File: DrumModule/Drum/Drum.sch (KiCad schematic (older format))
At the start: 44 parts, among them J1 Barrel_Jack_Switch, J2 Barrel_Jack_Switch, J3 Conn_02x05_Odd_Even, J4 Barrel_Jack_Switch, J5 Barrel_Jack_Switch, Q1 MMBT3904, Q2 MMBT3904, U1 74HC74, U2 MIC5205-5.0YM5, U3 LM2904DR, U4 LM2904DR

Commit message: Worked on the Drum
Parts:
- removed C10, C11, C4, C5: 1uF, Capacitor_SMD:C_0805_2012Metric, symbol Device:C_Small
- removed C6, C8: 68nF, Capacitor_SMD:C_0805_2012Metric, symbol Device:C_Small
- removed C7, C9: 22nF, Capacitor_SMD:C_0805_2012Metric, symbol Device:C_Small
- removed J1, J2, J4, J5: Barrel_Jack_Switch, Eurocad:PJ301M-12, symbol Connector:Barrel_Jack_Switch
- removed Q1, Q2: MMBT3904, Package_TO_SOT_SMD:SOT-23, symbol Transistor_BJT:MMBT3904
- removed R1, R2: 100k, Resistor_SMD:R_0805_2012Metric, symbol Device:R_US
- removed R10, R15, R16, R17, R18, R5, R6, R7, R8, R9: 10k, Resistor_SMD:R_0805_2012Metric, symbol Device:R_US
- removed R11, R3, R4: 1M, Resistor_SMD:R_0805_2012Metric, symbol Device:R_US
- removed R12: 2k2, Resistor_SMD:R_0805_2012Metric, symbol Device:R_US
- removed R13: 4.7M, Resistor_SMD:R_0805_2012Metric, symbol Device:R_US
- removed R14: 1k, Resistor_SMD:R_0805_2012Metric, symbol Device:R_US
- removed unit 1 of U1
- removed unit 2 of U1
- removed U3, U4: LM2904DR, Package_SO:SOIC-8_3.9x4.9mm_P1.27mm, symbol Device:Opamp_Dual_Generic
- U2: symbol Regulator_Linear:MIC5205-5.0YM5 -> Drum-rescue:MIC5205-5.0YM5-Regulator_Linear
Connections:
- wire segments 180 -> 56

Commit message: Organized layout of drum, should be ready for routing.
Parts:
- removed C2: 1uF, Capacitor_SMD:C_0805_2012Metric, symbol Device:C_Small
- removed U1: 74HC74, Package_SO:SOIC-14_3.9x8.7mm_P1.27mm, symbol 74xx:74HC74
- U2: symbol Drum-rescue:MIC5205-5.0YM5-Regulator_Linear -> Drum-rescue:MIC5205-5.0YM5-Regulator_Linear-Drum-rescue
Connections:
- wire segments 56 -> 48
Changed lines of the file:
@@
 $EndDescr
 $Comp
-L 74xx:74HC74 U1
-U 3 1 5C782298
-P 2400 6500
-F 0 "U1" V 2050 6400 50  0000 L CNN
-F 1 "74HC74" V 2150 6350 50  0000 L CNN
-F 2 "Package_SO:SOIC-14_3.9x8.7mm_P1.27mm" H 2400 6500 50  0001 C CNN
-F 3 "74xx/74hc_hct74.pdf" H 2400 6500 50  0001 C CNN
-	3    2400 6500
-	1    0    0    -1
-$EndComp
-$Comp
-L Drum-rescue:MIC5205-5.0YM5-Regulator_Linear U2
+L Drum-rescue:MIC5205-5.0YM5-Regulator_Linear-Drum-rescue U2
 U 1 1 5C78249B
 P 2950 4950
@@
 	1    0    0    -1
 $EndComp
-Wire Wire Line
-	2400 6100 2400 6050
-Wire Wire Line
-	2400 6900 2400 6950
-$Comp
-L power:GND #PWR011
-U 1 1 5C784795
-P 2400 7150
-F 0 "#PWR011" H 2400 6900 50  0001 C CNN
-F 1 "GND" H 2405 6977 50  0000 C CNN
-F 2 "" H 2400 7150 50  0001 C CNN
-F 3 "" H 2400 7150 50  0001 C CNN
-	1    2400 7150
-	1    0    0    -1
-$EndComp
-Wire Wire Line
-	2400 6950 2750 6950
-Connection ~ 2400 6950
-Wire Wire Line
-	2400 6950 2400 7150
-Wire Wire Line
-	2750 6050 2400 6050
-Connection ~ 2400 6050
-Wire Wire Line
-	2400 6050 2400 5850
 Wire Wire Line
 	1200 5900 1200 6000
@@
 $EndComp
 $Comp
-L power:+5V #PWR010
-U 1 1 5C79170B
-P 2400 5850
-F 0 "#PWR010" H 2400 5700 50  0001 C CNN
-F 1 "+5V" H 2415 6023 50  0000 C CNN
-F 2 "" H 2400 5850 50  0001 C CNN
-F 3 "" H 2400 5850 50  0001 C CNN
-	1    2400 5850
-	1    0    0    -1
-$EndComp
-$Comp
-L Device:C_Small C2
-U 1 1 5C791734
-P 2750 6450
-F 0 "C2" H 2842 6496 50  0000 L CNN
-F 1 "1uF" H 2842 6405 50  0000 L CNN
-F 2 "Capacitor_SMD:C_0805_2012Metric" H 2750 6450 50  0001 C CNN
-F 3 "~" H 2750 6450 50  0001 C CNN
-	1    2750 6450
-	1    0    0    -1
-$EndComp
-Wire Wire Line
-	2750 6050 2750 6350
-Wire Wire Line
-	2750 6550 2750 6950
-$Comp
 L power:GND #PWR016

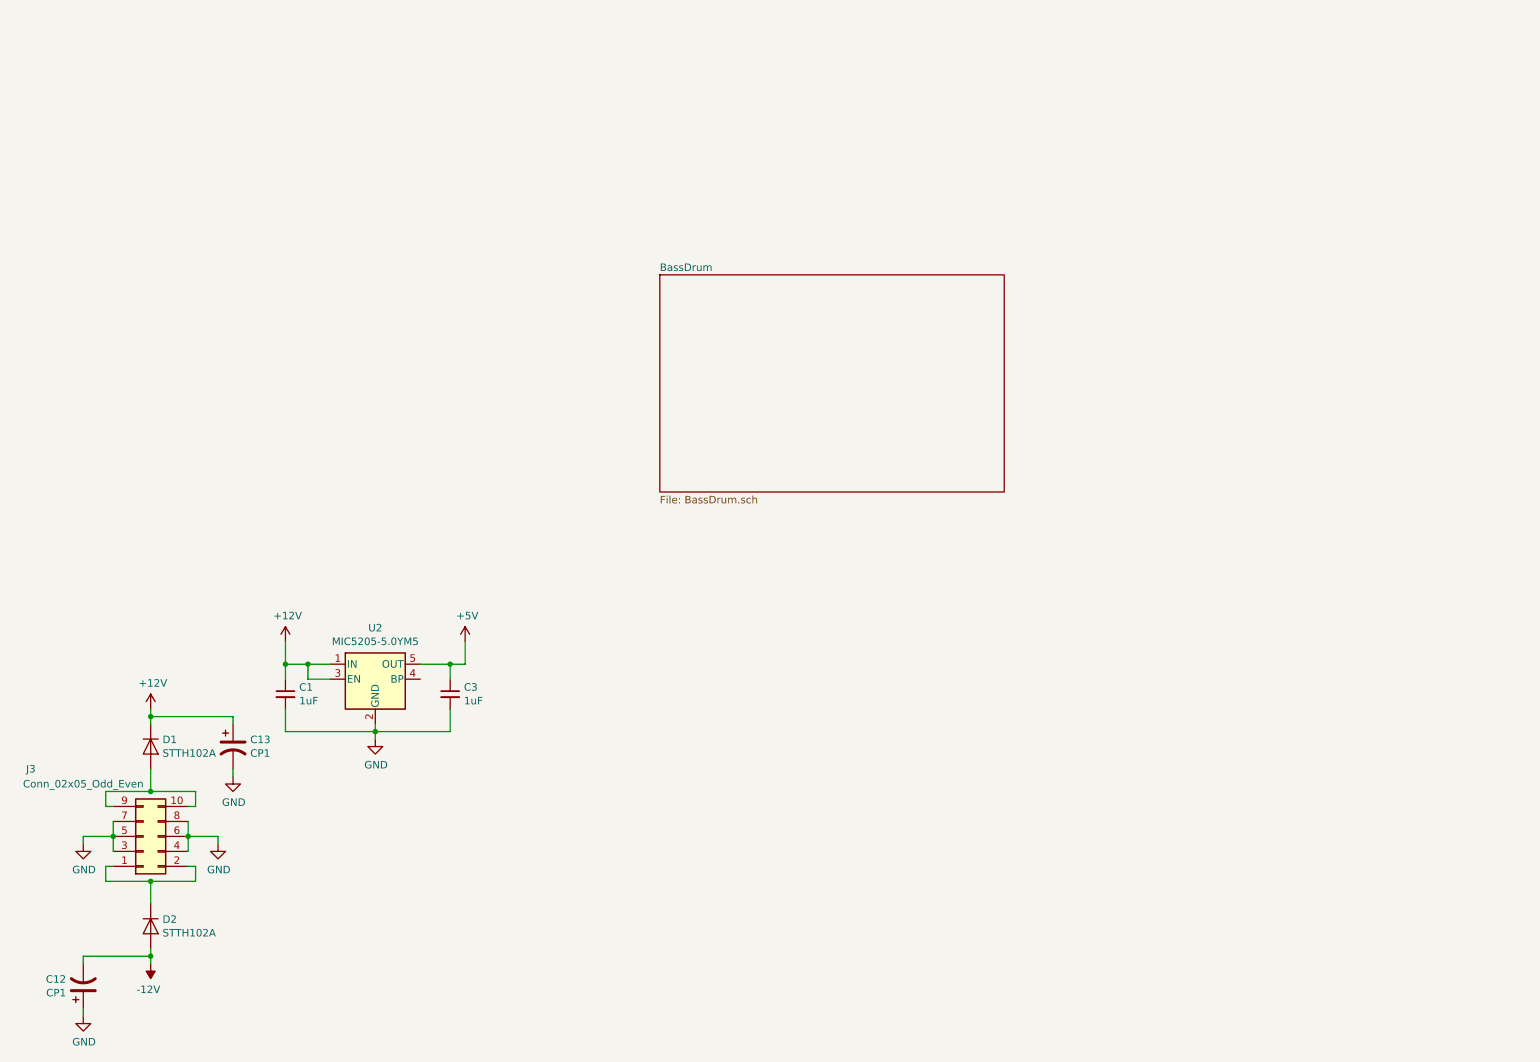
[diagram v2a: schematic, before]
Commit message: Finished off the drum
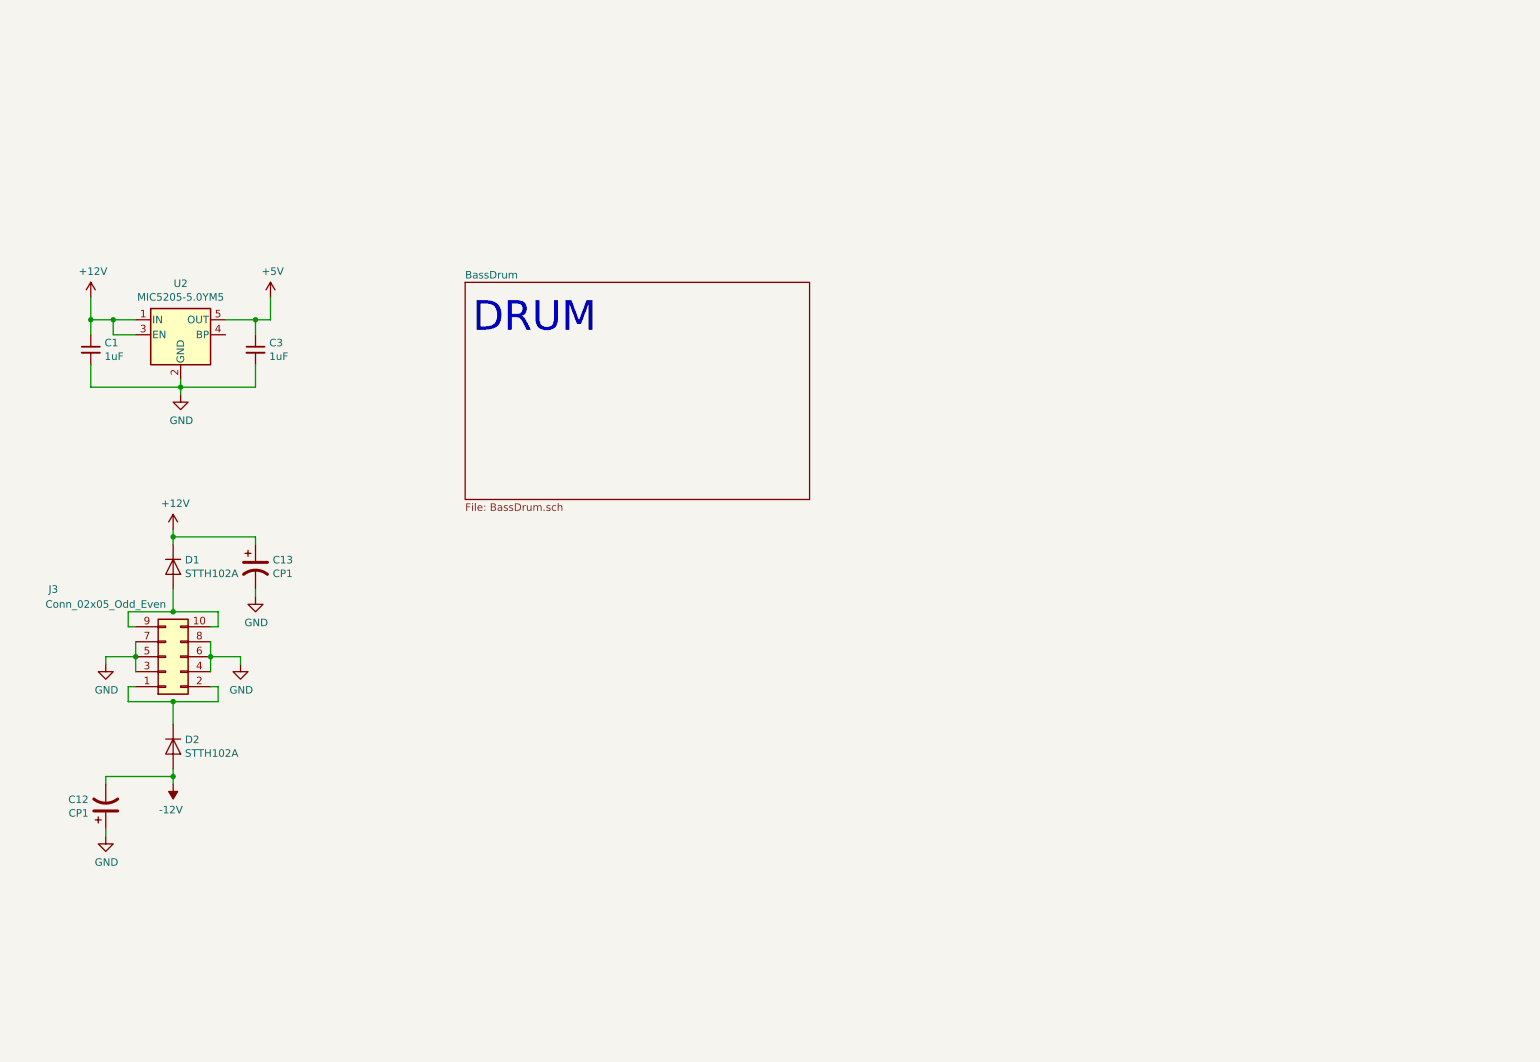
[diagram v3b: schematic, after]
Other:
- note added: "DRUM"
- moved on the sheet: C1, C12, C13, C3, D1, D2, J3, U2

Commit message: Updated parts for the Bob bass
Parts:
- U2: symbol Drum-rescue:MIC5205-5.0YM5-Regulator_Linear-Drum-rescue -> Drum-rescue:MIC5205-5.0YM5-Regulator_Linear-Drum-rescue-Drum-rescue
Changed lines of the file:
@@
 $EndDescr
 $Comp
-L Drum-rescue:MIC5205-5.0YM5-Regulator_Linear-Drum-rescue U2
+L Drum-rescue:MIC5205-5.0YM5-Regulator_Linear-Drum-rescue-Drum-rescue U2
 U 1 1 5C78249B
 P 1650 2650
